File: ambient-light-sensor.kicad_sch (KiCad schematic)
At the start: 5 parts, among them Q1 TEPT4400

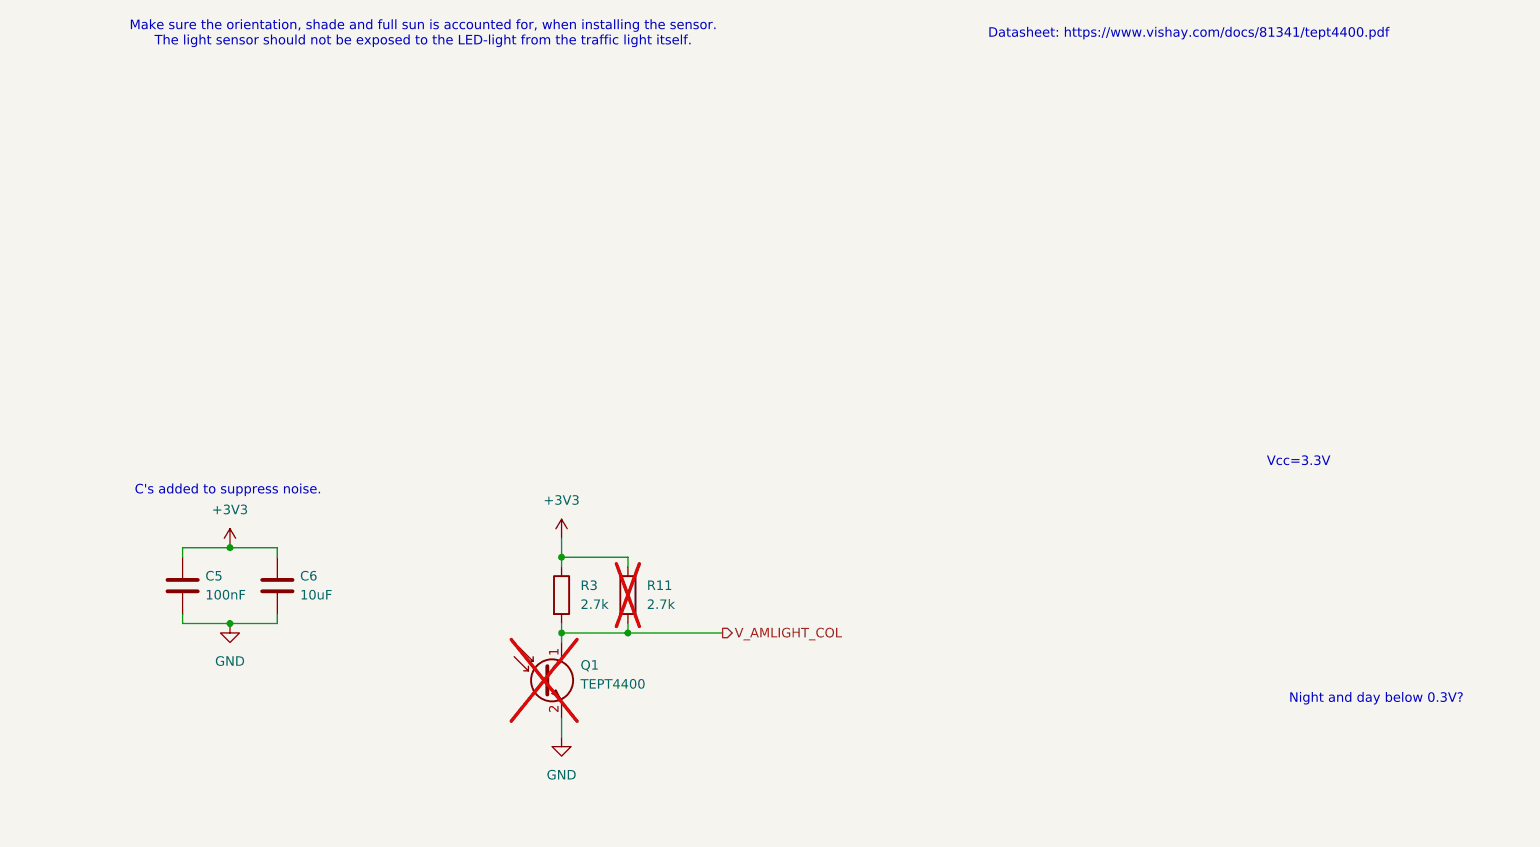
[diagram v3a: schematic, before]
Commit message: Changed capacitors to span the TEPT4400
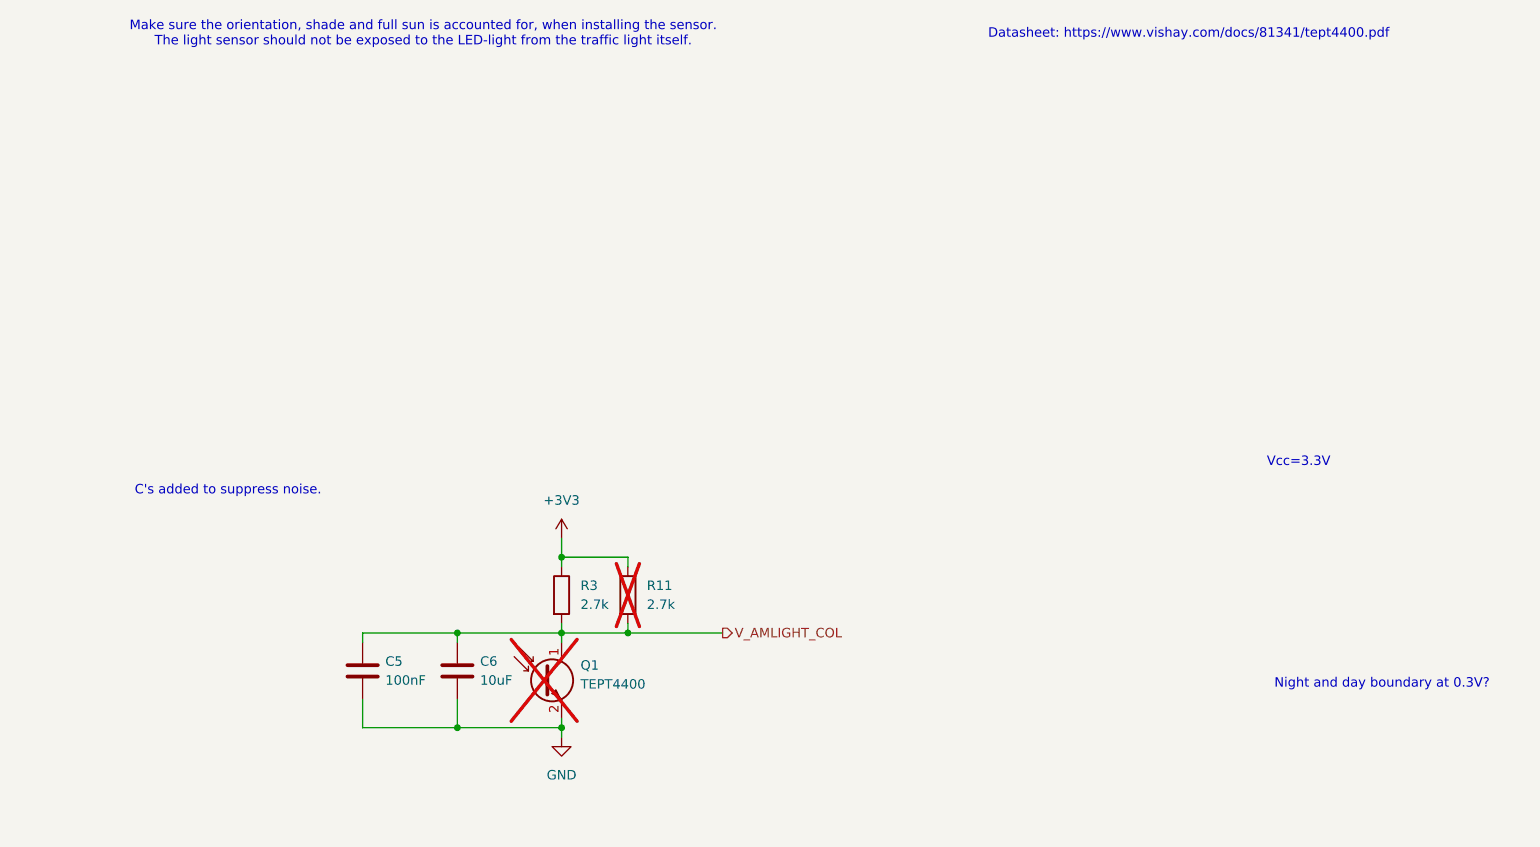
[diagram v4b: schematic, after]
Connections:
- net +3V3: no longer C5.1, C6.1
- net V_AMLIGHT_COL: now also C5.1, C6.1
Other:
- note added: "Night and day boundary at 0.3V?"
- note removed: "Night and day below 0.3V?"
- moved on the sheet: C5, C6
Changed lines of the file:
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@@
 	(generator_version "9.0")
 	(paper "A4")
-	(text "Night and day below 0.3V?"
+	(text "Night and day boundary at 0.3V?"
 		(exclude_from_sim no)
-		(at 234.95 110.49 0)
+		(at 235.712 108.458 0)
 		(effects
 			(font
@@
 	)
 	(junction
-		(at 81.28 90.17)
+		(at 125.73 114.3)
+		(diameter 0)
+		(color 0 0 0 0)
+	)
+	(junction
+		(at 111.76 114.3)
 		(diameter 0)
 		(color 0 0 0 0)
@@
 	)
 	(junction
-		(at 81.28 100.33)
+		(at 125.73 101.6)
 		(diameter 0)
 		(color 0 0 0 0)
 	)
 	(junction
-		(at 125.73 101.6)
+		(at 111.76 101.6)
 		(diameter 0)
 		(color 0 0 0 0)
@@
 	(wire
 		(pts
-			(xy 74.93 100.33) (xy 81.28 100.33)
+			(xy 134.62 92.71) (xy 134.62 91.44)
 		)
 		(stroke
@@
 	(wire
 		(pts
-			(xy 134.62 92.71) (xy 134.62 91.44)
+			(xy 99.06 110.49) (xy 99.06 114.3)
 		)
 		(stroke
@@
 	(wire
 		(pts
-			(xy 74.93 99.06) (xy 74.93 100.33)
+			(xy 99.06 101.6) (xy 99.06 102.87)
 		)
 		(stroke
@@
 	(wire
 		(pts
-			(xy 74.93 90.17) (xy 74.93 91.44)
+			(xy 125.73 101.6) (xy 125.73 102.87)
 		)
 		(stroke
@@
 	(wire
 		(pts
-			(xy 74.93 90.17) (xy 81.28 90.17)
+			(xy 134.62 100.33) (xy 134.62 101.6)
 		)
 		(stroke
@@
 	(wire
 		(pts
-			(xy 125.73 101.6) (xy 125.73 102.87)
+			(xy 99.06 114.3) (xy 111.76 114.3)
 		)
 		(stroke
@@
 	(wire
 		(pts
-			(xy 134.62 100.33) (xy 134.62 101.6)
+			(xy 125.73 92.71) (xy 125.73 91.44)
 		)
 		(stroke
@@
 	(wire
 		(pts
-			(xy 81.28 100.33) (xy 87.63 100.33)
+			(xy 125.73 114.3) (xy 125.73 115.57)
 		)
 		(stroke
@@
 	(wire
 		(pts
-			(xy 125.73 92.71) (xy 125.73 91.44)
+			(xy 99.06 101.6) (xy 111.76 101.6)
 		)
 		(stroke
@@
 	(wire
 		(pts
-			(xy 81.28 90.17) (xy 87.63 90.17)
+			(xy 125.73 101.6) (xy 134.62 101.6)
 		)
 		(stroke
@@
 	(wire
 		(pts
-			(xy 125.73 101.6) (xy 134.62 101.6)
+			(xy 111.76 110.49) (xy 111.76 114.3)
 		)
 		(stroke
@@
 	(wire
 		(pts
-			(xy 87.63 99.06) (xy 87.63 100.33)
+			(xy 125.73 88.9) (xy 125.73 91.44)
 		)
 		(stroke
@@
 	(wire
 		(pts
-			(xy 125.73 88.9) (xy 125.73 91.44)
+			(xy 111.76 114.3) (xy 125.73 114.3)
 		)
 		(stroke
@@
 	(wire
 		(pts
-			(xy 125.73 113.03) (xy 125.73 115.57)
+			(xy 125.73 113.03) (xy 125.73 114.3)
 		)
 		(stroke
@@
 	(wire
 		(pts
-			(xy 87.63 90.17) (xy 87.63 91.44)
+			(xy 111.76 101.6) (xy 111.76 102.87)
 		)
 		(stroke
@@
 	(wire
 		(pts
+			(xy 111.76 101.6) (xy 125.73 101.6)
+		)
+		(stroke
+			(width 0)
+			(type default)
+		)
+	)
+	(wire
+		(pts
 			(xy 125.73 100.33) (xy 125.73 101.6)
 		)
@@
 	(symbol
 		(lib_id "Device:C")
-		(at 74.93 95.25 0)
+		(at 99.06 106.68 0)
 		(unit 1)
 		(exclude_from_sim no)
@@
 		(dnp no)
 		(property "Reference" "C5"
-			(at 77.978 93.98 0)
+			(at 102.108 105.41 0)
 			(effects
 				(font
@@
 		)
 		(property "Value" "100nF"
-			(at 77.978 96.52 0)
+			(at 102.108 107.95 0)
 			(effects
 				(font
@@
 		)
 		(property "Footprint" "Capacitor_SMD:C_0805_2012Metric"
-			(at 75.8952 99.06 0)
+			(at 100.0252 110.49 0)
 			(effects
 				(font
@@
 		)
 		(property "Datasheet" "https://jlcpcb.com/partdetail/YAGEO-CC0603KRX7R9BB104/C14663"
-			(at 74.93 95.25 0)
+			(at 99.06 106.68 0)
 			(effects
 				(font
@@
 		)
 		(property "Description" "Unpolarized capacitor"
-			(at 74.93 95.25 0)
+			(at 99.06 106.68 0)
 			(effects
 				(font
@@
 		)
 		(property "LCSC" "C14663"
-			(at 74.93 95.25 0)
+			(at 99.06 106.68 0)
 			(effects
 				(font
@@
 	)
 	(symbol
-		(lib_id "power:GND")
-		(at 81.28 100.33 0)
-		(unit 1)
-		(exclude_from_sim no)
-		(in_bom yes)
-		(on_board yes)
-		(dnp no)
-		(fields_autoplaced yes)
-		(property "Reference" "#PWR054"
-			(at 81.28 106.68 0)
-			(effects
-				(font
-					(size 1.27 1.27)
-				)
-				(hide yes)
-			)
-		)
-		(property "Value" "GND"
-			(at 81.28 105.41 0)
-			(effects
-				(font
-					(size 1.27 1.27)
-				)
-			)
-		)
-		(property "Footprint" ""
-			(at 81.28 100.33 0)
-			(effects
-				(font
-					(size 1.27 1.27)
-				)
-				(hide yes)
-			)
-		)
-		(property "Datasheet" ""
-			(at 81.28 100.33 0)
-			(effects
-				(font
-					(size 1.27 1.27)
-				)
-				(hide yes)
-			)
-		)
-		(property "Description" "Power symbol creates a global label with name \"GND\" , ground"
-			(at 81.28 100.33 0)
-			(effects
-				(font
-					(size 1.27 1.27)
-				)
-				(hide yes)
-			)
-		)
-		(pin "1"
-		)
-		(instances
-			(project "stopnu-hardware"
-				(path "/4ab90003-ea4c-4878-8117-f834ac24f8d9/7b0869a3-a922-42ed-84a7-59d61dea9664"
-					(reference "#PWR054")
-					(unit 1)
-				)
-			)
-		)
-	)
-	(symbol
 		(lib_id "Device:R")
 		(at 125.73 96.52 0)
@@
 	(symbol
 		(lib_id "power:+3V3")
-		(at 81.28 90.17 0)
-		(unit 1)
-		(exclude_from_sim no)
-		(in_bom yes)
-		(on_board yes)
-		(dnp no)
-		(fields_autoplaced yes)
-		(property "Reference" "#PWR053"
-			(at 81.28 93.98 0)
-			(effects
-				(font
-					(size 1.27 1.27)
-				)
-				(hide yes)
-			)
-		)
-		(property "Value" "+3V3"
-			(at 81.28 85.09 0)
-			(effects
-				(font
-					(size 1.27 1.27)
-				)
-			)
-		)
-		(property "Footprint" ""
-			(at 81.28 90.17 0)
-			(effects
-				(font
-					(size 1.27 1.27)
-				)
-				(hide yes)
-			)
-		)
-		(property "Datasheet" ""
-			(at 81.28 90.17 0)
-			(effects
-				(font
-					(size 1.27 1.27)
-				)
-				(hide yes)
-			)
-		)
-		(property "Description" "Power symbol creates a global label with name \"+3V3\""
-			(at 81.28 90.17 0)
-			(effects
-				(font
-					(size 1.27 1.27)
-				)
-				(hide yes)
-			)
-		)
-		(pin "1"
-		)
-		(instances
-			(project "stopnu-hardware"
-				(path "/4ab90003-ea4c-4878-8117-f834ac24f8d9/7b0869a3-a922-42ed-84a7-59d61dea9664"
-					(reference "#PWR053")
-					(unit 1)
-				)
-			)
-		)
-	)
-	(symbol
-		(lib_id "power:+3V3")
 		(at 125.73 88.9 0)
 		(unit 1)
@@
 	(symbol
 		(lib_id "Device:C")
-		(at 87.63 95.25 0)
+		(at 111.76 106.68 0)
 		(unit 1)
 		(exclude_from_sim no)
@@
 		(dnp no)
 		(property "Reference" "C6"
-			(at 90.678 93.98 0)
+			(at 114.808 105.41 0)
 			(effects
 				(font
@@
 		)
 		(property "Value" "10uF"
-			(at 90.678 96.52 0)
+			(at 114.808 107.95 0)
 			(effects
 				(font
@@
 		)
 		(property "Footprint" "Capacitor_SMD:C_0805_2012Metric"
-			(at 88.5952 99.06 0)
+			(at 112.7252 110.49 0)
 			(effects
 				(font
@@
 		)
 		(property "Datasheet" "https://jlcpcb.com/partdetail/2065-CL21A106KOQNNNE/C1713"
-			(at 87.63 95.25 0)
+			(at 111.76 106.68 0)
 			(effects
 				(font
@@
 		)
 		(property "Description" "Unpolarized capacitor"
-			(at 87.63 95.25 0)
+			(at 111.76 106.68 0)
 			(effects
 				(font
@@
 		)
 		(property "LCSC" "C1713"
-			(at 87.63 95.25 0)
+			(at 111.76 106.68 0)
 			(effects
 				(font

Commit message: Fixed fabrication files, so PCBA will work with the correct rotation of the components.
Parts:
- C5: LCSC C14663 -> C49678
- C6: LCSC C1713 -> C440198
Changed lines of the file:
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@@
 			)
 		)
-		(property "Datasheet" "https://jlcpcb.com/partdetail/YAGEO-CC0603KRX7R9BB104/C14663"
+		(property "Datasheet" "https://jlcpcb.com/partdetail/YAGEO-CC0805KRX7R9BB104/C49678"
 			(at 99.06 106.68 0)
 			(effects
@@
 			)
 		)
-		(property "LCSC" "C14663"
+		(property "LCSC" "C49678"
+			(at 99.06 106.68 0)
+			(effects
+				(font
+					(size 1.27 1.27)
+				)
+				(hide yes)
+			)
+		)
+		(property "gnd" ""
+			(at 99.06 106.68 0)
+			(effects
+				(font
+					(size 1.27 1.27)
+				)
+				(hide yes)
+			)
+		)
+		(property "input1" ""
+			(at 99.06 106.68 0)
+			(effects
+				(font
+					(size 1.27 1.27)
+				)
+				(hide yes)
+			)
+		)
+		(property "input2" ""
+			(at 99.06 106.68 0)
+			(effects
+				(font
+					(size 1.27 1.27)
+				)
+				(hide yes)
+			)
+		)
+		(property "input3" ""
 			(at 99.06 106.68 0)
 			(effects
@@
 			)
 		)
+		(property "gnd" ""
+			(at 125.73 96.52 0)
+			(effects
+				(font
+					(size 1.27 1.27)
+				)
+				(hide yes)
+			)
+		)
+		(property "input1" ""
+			(at 125.73 96.52 0)
+			(effects
+				(font
+					(size 1.27 1.27)
+				)
+				(hide yes)
+			)
+		)
+		(property "input2" ""
+			(at 125.73 96.52 0)
+			(effects
+				(font
+					(size 1.27 1.27)
+				)
+				(hide yes)
+			)
+		)
+		(property "input3" ""
+			(at 125.73 96.52 0)
+			(effects
+				(font
+					(size 1.27 1.27)
+				)
+				(hide yes)
+			)
+		)
 		(pin "1"
 		)
@@
 			)
 		)
+		(property "gnd" ""
+			(at 123.19 107.95 0)
+			(effects
+				(font
+					(size 1.27 1.27)
+				)
+				(hide yes)
+			)
+		)
+		(property "input1" ""
+			(at 123.19 107.95 0)
+			(effects
+				(font
+					(size 1.27 1.27)
+				)
+				(hide yes)
+			)
+		)
+		(property "input2" ""
+			(at 123.19 107.95 0)
+			(effects
+				(font
+					(size 1.27 1.27)
+				)
+				(hide yes)
+			)
+		)
+		(property "input3" ""
+			(at 123.19 107.95 0)
+			(effects
+				(font
+					(size 1.27 1.27)
+				)
+				(hide yes)
+			)
+		)
 		(pin "2"
 		)
@@
 			)
 		)
-		(property "Datasheet" "https://jlcpcb.com/partdetail/2065-CL21A106KOQNNNE/C1713"
+		(property "Datasheet" "https://jlcpcb.com/partdetail/439567-GRM21BR61H106KE43L/C440198"
 			(at 111.76 106.68 0)
 			(effects
@@
 			)
 		)
-		(property "LCSC" "C1713"
+		(property "LCSC" "C440198"
+			(at 111.76 106.68 0)
+			(effects
+				(font
+					(size 1.27 1.27)
+				)
+				(hide yes)
+			)
+		)
+		(property "gnd" ""
+			(at 111.76 106.68 0)
+			(effects
+				(font
+					(size 1.27 1.27)
+				)
+				(hide yes)
+			)
+		)
+		(property "input1" ""
+			(at 111.76 106.68 0)
+			(effects
+				(font
+					(size 1.27 1.27)
+				)
+				(hide yes)
+			)
+		)
+		(property "input2" ""
+			(at 111.76 106.68 0)
+			(effects
+				(font
+					(size 1.27 1.27)
+				)
+				(hide yes)
+			)
+		)
+		(property "input3" ""
 			(at 111.76 106.68 0)
 			(effects
@@
 			(at 134.62 96.52 0)
 			(effects
+				(font
+					(size 1.27 1.27)
+				)
+				(hide yes)
+			)
+		)
+		(property "gnd" ""
+			(at 134.62 96.52 0)
+			(effects
+				(font
+					(size 1.27 1.27)
+				)
+				(hide yes)
+			)
+		)
+		(property "input1" ""
+			(at 134.62 96.52 0)
+			(effects
+				(font
+					(size 1.27 1.27)
+				)
+				(hide yes)
+			)
+		)
+		(property "input2" ""
+			(at 134.62 96.52 0)
+			(effects
+				(font
+					(size 1.27 1.27)
+				)
+				(hide yes)
+			)
+		)
+		(property "input3" ""
+			(at 134.62 96.52 0)
+			(effects
